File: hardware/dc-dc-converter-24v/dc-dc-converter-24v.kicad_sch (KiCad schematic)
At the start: 8 parts, among them J1 24V, J2 12V, J3 GND, J4 GND

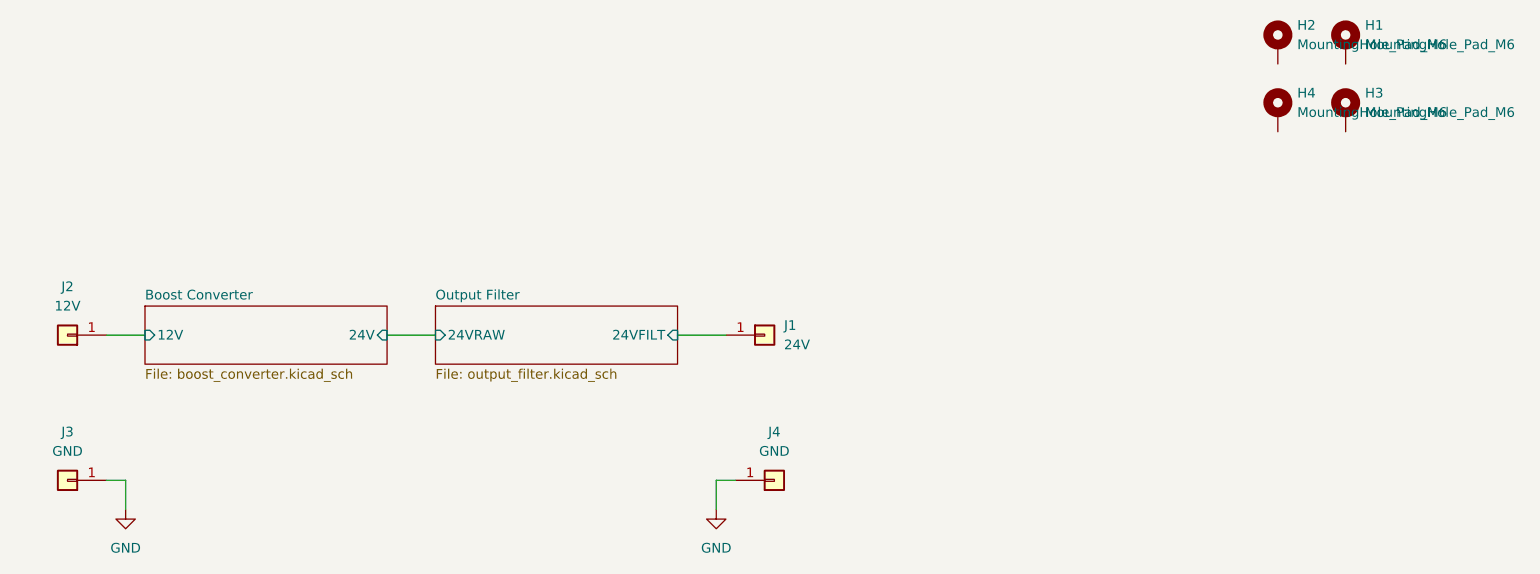
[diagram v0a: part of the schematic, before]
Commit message: create layout for DC-DC converter
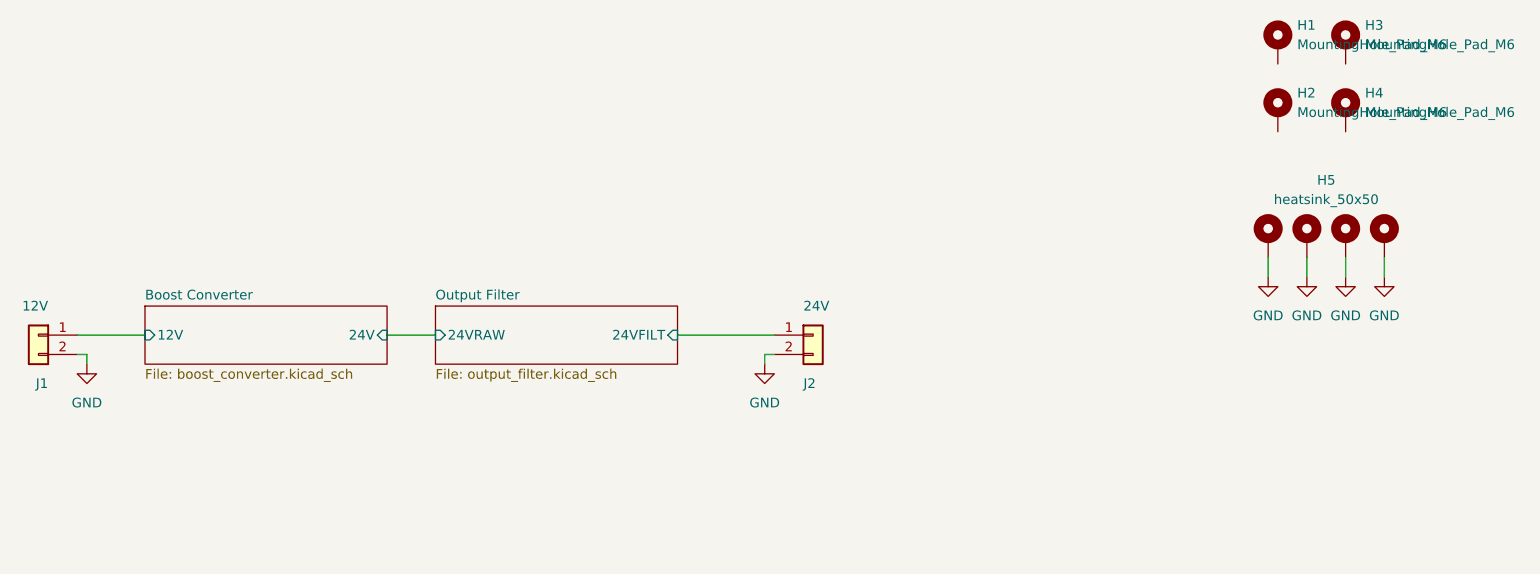
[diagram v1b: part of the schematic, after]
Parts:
- removed J1: 24V, benediktibk:Connector_M6, symbol benediktibk:Connector_M6
- removed J2: 12V, benediktibk:Connector_M6, symbol benediktibk:Connector_M6
- removed J3, J4: GND, benediktibk:Connector_M6, symbol benediktibk:Connector_M6
- added H5: heatsink_50x50, benediktibk:heatsink_50x50, symbol benediktibk:heatsink_50x50
- added J1: 12V, benediktibk:rspro_header_2pin_5_08mm, symbol benediktibk:rspro_header_2pin_5_08mm
- added J2: 24V, benediktibk:rspro_header_2pin_5_08mm, symbol benediktibk:rspro_header_2pin_5_08mm
- renumbered H2 to H1, H4 to H2, H1 to H3, H3 to H4
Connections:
- net Boost Converter/12V: now also J1.1 (Pin_1)
- net GND: now also H5.1 (GND), H5.2 (GND), H5.3 (GND), H5.4 (GND), J1.2 (Pin_2), J2.2 (Pin_2)
- net Output Filter/24VFILT: now also J2.1 (Pin_1)

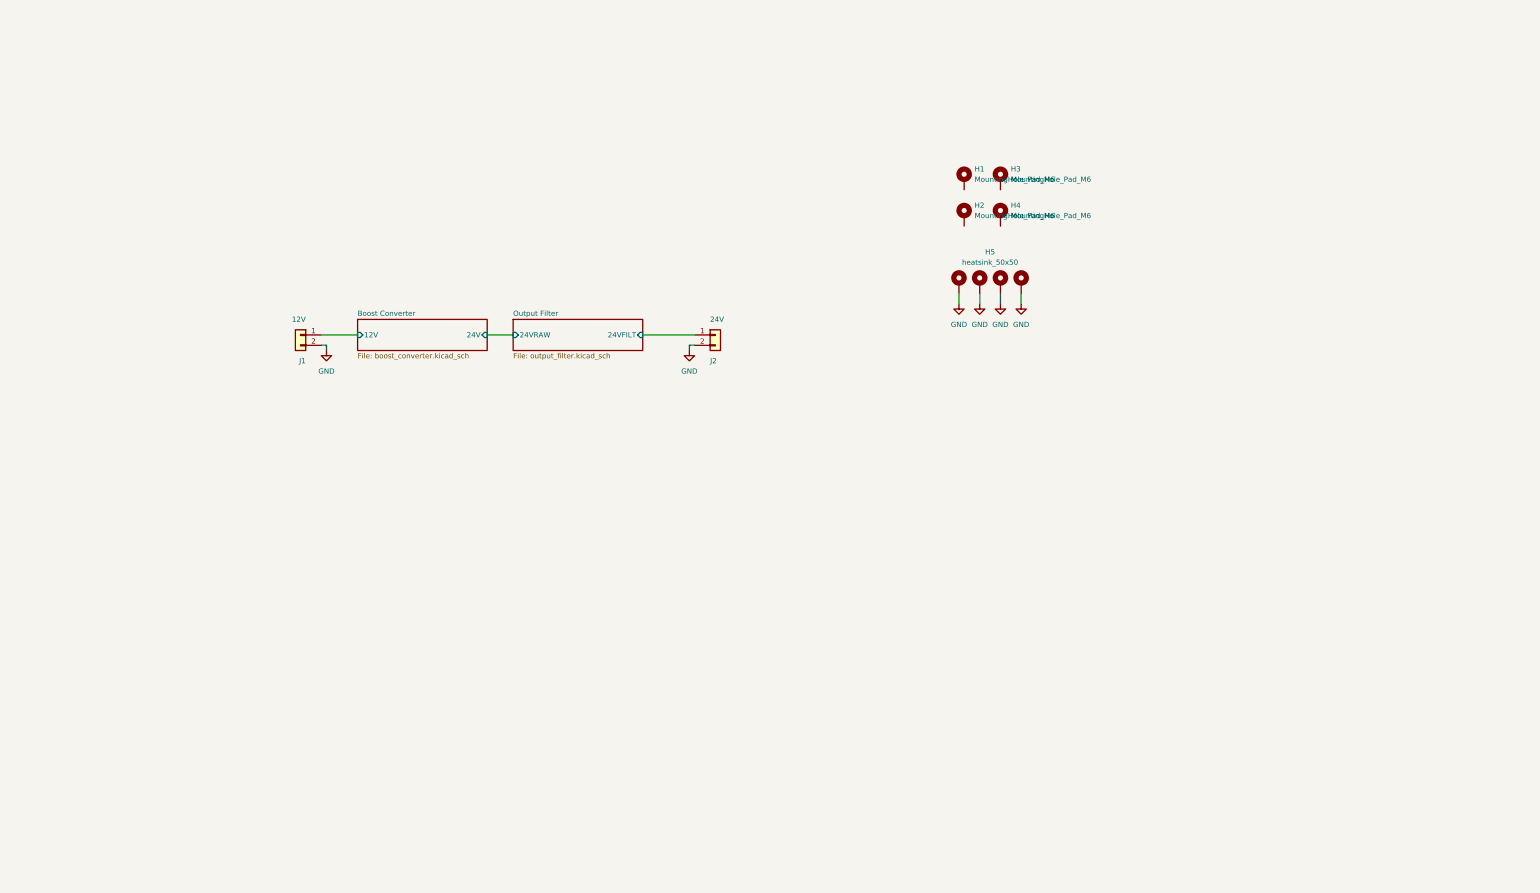
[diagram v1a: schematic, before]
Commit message: fix design errors in DC DC converter
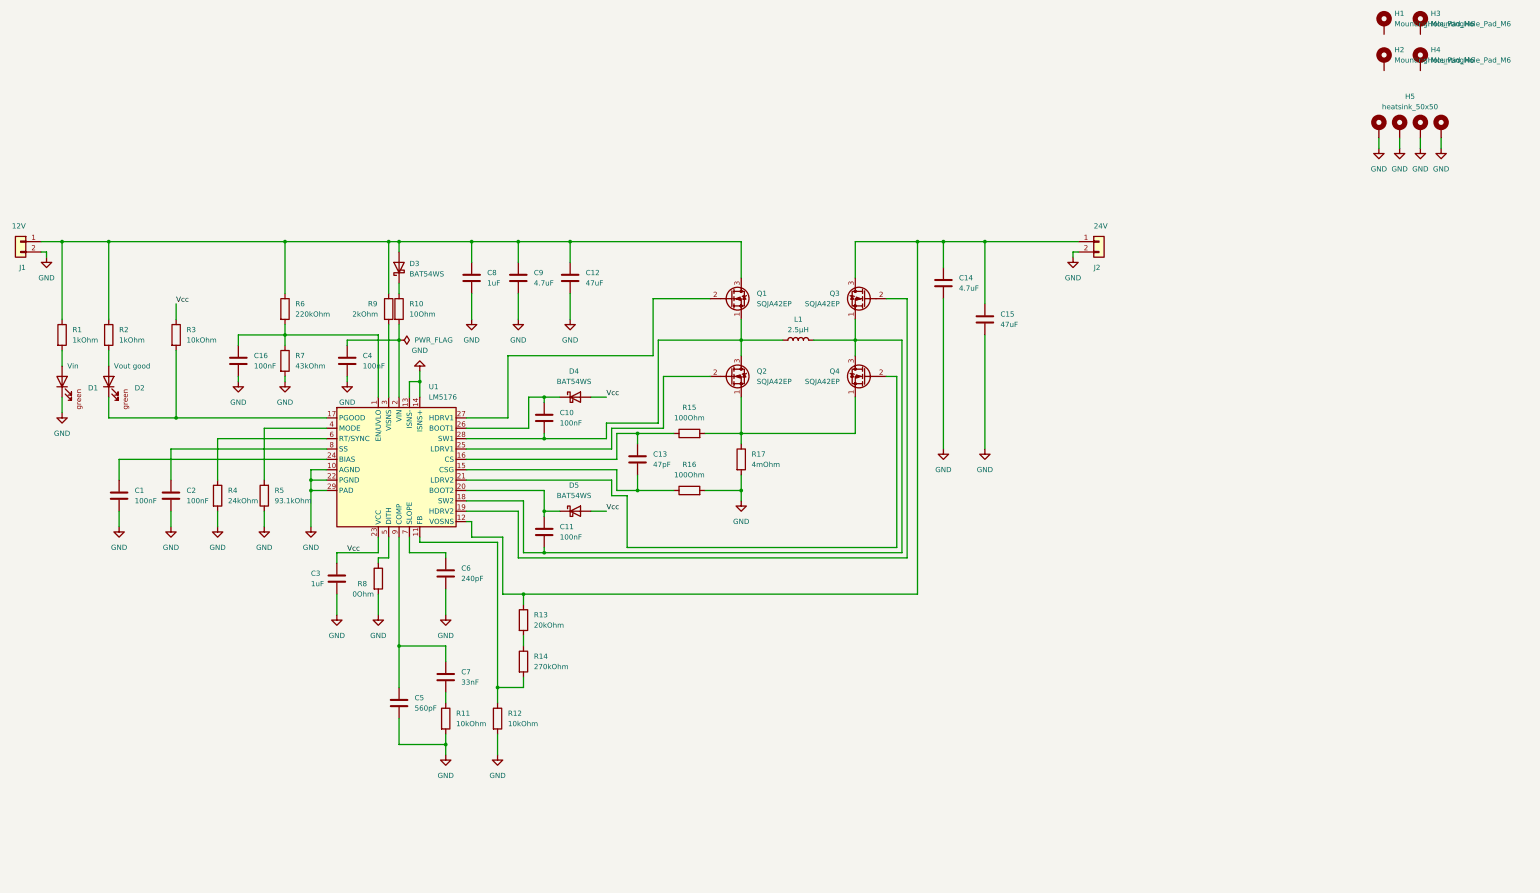
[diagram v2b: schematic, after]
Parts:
- added C1, C10, C11, C16, C2, C4: 100nF, benediktibk:C_0603_1608Metric_Pad1.08x0.95mm_HandSolder, symbol benediktibk:C_100nF_SMD_0603_50V
- added C12, C15: 47uF, benediktibk:C_1206_3216Metric_Pad1.33x1.80mm_HandSolder, symbol benediktibk:C_47uF_SMD_1206_25V_20%
- added C13: 47pF, benediktibk:C_0603_1608Metric_Pad1.08x0.95mm_HandSolder, symbol benediktibk:C_47pF_SMD_0603_100V_5%
- added C14, C9: 4.7uF, benediktibk:C_0805_2012Metric_Pad1.18x1.45mm_HandSolder, symbol benediktibk:C_4_7uF_SMD_0805_50V_10%
- added C3, C8: 1uF, benediktibk:C_0603_1608Metric_Pad1.08x0.95mm_HandSolder, symbol benediktibk:C_1uF_SMD_0603_50V_10%
- added C5: 560pF, benediktibk:C_0603_1608Metric_Pad1.08x0.95mm_HandSolder, symbol benediktibk:C_560pF_SMD_0603_50V_5%
- added C6: 240pF, benediktibk:C_0805_2012Metric_Pad1.18x1.45mm_HandSolder, symbol benediktibk:C_240pF_SMD_0805_250V_10%
- added C7: 33nF, benediktibk:C_0603_1608Metric_Pad1.08x0.95mm_HandSolder, symbol benediktibk:C_33nF_SMD_0603_50V_10%
- added D1: Vin, benediktibk:D_0603_1608Metric_Pad1.05x0.95mm_HandSolder, symbol benediktibk:LED_green_0603
- added D2: Vout good, benediktibk:D_0603_1608Metric_Pad1.05x0.95mm_HandSolder, symbol benediktibk:LED_green_0603
- added D3, D4, D5: BAT54WS, benediktibk:D_SOD-323, symbol benediktibk:BAT54WS
- added L1: 2.5µH, benediktibk:ETQP8, symbol benediktibk:L_2_5µH_30A
- added Q1, Q2, Q3, Q4: SQJA42EP, benediktibk:SQJA42EPT1_GE3, symbol benediktibk:SQJA42EP
- added R1, R2: 1kOhm, benediktibk:R_0603_1608Metric_Pad0.98x0.95mm_HandSolder, symbol benediktibk:R_1kOhm_SMD_0603_100mW_1%
- added R10: 10Ohm, benediktibk:R_0603_1608Metric_Pad0.98x0.95mm_HandSolder, symbol benediktibk:R_10Ohm_SMD_0603_100mW_1%
- added R11, R12, R3: 10kOhm, benediktibk:R_0603_1608Metric_Pad0.98x0.95mm_HandSolder, symbol benediktibk:R_10kOhm_SMD_0603_100mW_1%
- added R13: 20kOhm, benediktibk:R_0603_1608Metric_Pad0.98x0.95mm_HandSolder, symbol benediktibk:R_20kOhm_SMD_0603_100mW_1%
- added R14: 270kOhm, benediktibk:R_0603_1608Metric_Pad0.98x0.95mm_HandSolder, symbol benediktibk:R_270kOhm_SMD_0603_100mW_1%
- added R15, R16: 100Ohm, benediktibk:R_0603_1608Metric_Pad0.98x0.95mm_HandSolder, symbol benediktibk:R_100Ohm_SMD_0603_100mW_1%
- added R17: 4mOhm, benediktibk:R_2512_6332Metric_Pad1.40x3.35mm_HandSolder, symbol benediktibk:R_4mOhm_SMD_2512_2W_1%
- added R4: 24kOhm, benediktibk:R_0603_1608Metric_Pad0.98x0.95mm_HandSolder, symbol benediktibk:R_24kOhm_SMD_0603_100mW_1%
- added R5: 93.1kOhm, benediktibk:R_0603_1608Metric_Pad0.98x0.95mm_HandSolder, symbol benediktibk:R_93_1kOhm_SMD_0603_100mW_0_1%
- added R6: 220kOhm, benediktibk:R_0603_1608Metric_Pad0.98x0.95mm_HandSolder, symbol benediktibk:R_220kOhm_SMD_0603_100mW_1%
- added R7: 43kOhm, benediktibk:R_0603_1608Metric_Pad0.98x0.95mm_HandSolder, symbol benediktibk:R_43kOhm_SMD_0603_100mW_1%
- added R8: 0Ohm, benediktibk:R_0603_1608Metric_Pad0.98x0.95mm_HandSolder, symbol benediktibk:R_0Ohm_SMD_0603_100mW_0%
- added R9: 2kOhm, benediktibk:R_0603_1608Metric_Pad0.98x0.95mm_HandSolder, symbol benediktibk:R_2kOhm_SMD_0603_100mW_1%
- added U1: LM5176, benediktibk:LM5176, symbol benediktibk:LM5176
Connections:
- net GND: now also C1.2, C12.2, C14.2, C15.2, C16.2, C2.2, C3.2, C4.2, C5.2, C6.2, C8.2, C9.2, D1.1 (K), R11.2, R12.2, R16.2, R17.2, R4.2, R5.1, R7.2, R8.2, U1.10 (AGND), U1.13 (ISNS-), U1.14 (ISNS+), U1.22 (PGND), U1.29 (PAD)
- net Boost Converter/12V: no longer names the net of J1.1 (Pin_1)
- net Boost Converter/12V: now also C12.1, C8.1, C9.1, D3.2 (A), Q1.3 (D), R1.1, R2.1, R6.1, R9.1
- net Output Filter/24VFILT: no longer names the net of J2.1 (Pin_1)
- net Output Filter/24VFILT: now also C14.1, C15.1, Q3.3 (D), R13.1, U1.12 (VOSNS)
- new net: Q2.1 (S), Q4.1 (S), R15.2, R17.1
- new net: R9.2, U1.3 (VISNS)
- new net: D2.2 (A), R2.2
- new net: C11.1, D5.1 (K), U1.20 (BOOT2)
- new net: C5.1, C7.1, U1.9 (COMP)
- new net: C16.1, R6.2, R7.1, U1.1 (EN/UVLO)
- new net: C4.1, R10.2, U1.2 (VIN)
- new net: R13.2, R14.1
- new net: C7.2, R11.1
- new net: D1.2 (A), R1.2
- new net: R5.2, U1.4 (MODE)
- new net: C10.1, D4.1 (K), U1.26 (BOOT1)
- new net: R12.1, R14.2, U1.11 (FB)
- new net: C13.2, R16.1, U1.15 (CSG)
- new net: C2.1, U1.8 (SS)
- new net: D2.1 (K), R3.2, U1.17 (PGOOD)
- new net: C13.1, R15.1, U1.16 (CS)
- new net: C11.2, L1.2, Q3.1 (S), Q4.3 (D), U1.18 (SW2)
- new net: D3.1 (K), R10.1
- new net: C6.1, U1.7 (SLOPE)
- new net: C10.2, L1.1, Q1.1 (S), Q2.3 (D), U1.28 (SW1)
- new net: Q1.2 (G), U1.27 (HDRV1)
- new net: R4.1, U1.6 (RT/SYNC)
- new net: Q3.2 (G), U1.19 (HDRV2)
- new net: Q4.2 (G), U1.21 (LDRV2)
- new net: Q2.2 (G), U1.25 (LDRV1)
- new net: C1.1, U1.24 (BIAS)
- new net: R8.1, U1.5 (DITH)
- new net Vcc: C3.1, D4.2 (A), D5.2 (A), R3.1, U1.23 (VCC)
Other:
- removed sheet Boost Converter
- removed sheet Output Filter
- moved on the sheet: H1, H2, H3, H4, H5, J1, J2

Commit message: start with redesign of DC DC converter
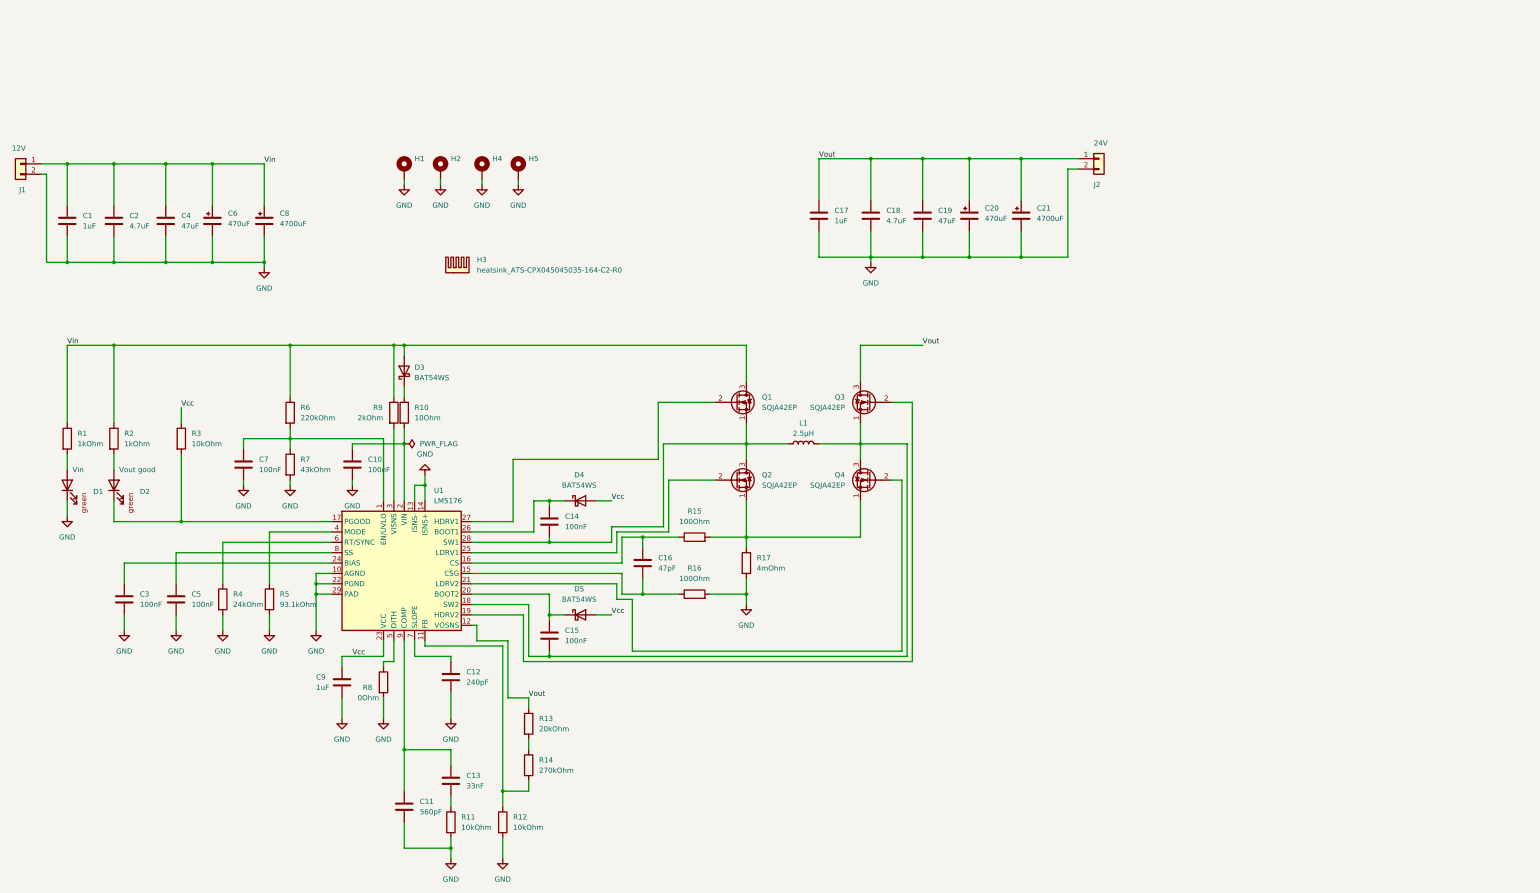
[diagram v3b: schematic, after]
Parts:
- removed C12: 47uF, benediktibk:C_1206_3216Metric_Pad1.33x1.80mm_HandSolder, symbol benediktibk:C_47uF_SMD_1206_25V_20%
- removed C8: 1uF, benediktibk:C_0603_1608Metric_Pad1.08x0.95mm_HandSolder, symbol benediktibk:C_1uF_SMD_0603_50V_10%
- removed C9: 4.7uF, benediktibk:C_0805_2012Metric_Pad1.18x1.45mm_HandSolder, symbol benediktibk:C_4_7uF_SMD_0805_50V_10%
- removed H5: heatsink_50x50, benediktibk:heatsink_50x50, symbol benediktibk:heatsink_50x50
- added C1, C17: 1uF, benediktibk:C_0603_1608Metric_Pad1.08x0.95mm_HandSolder, symbol benediktibk:C_1uF_SMD_0603_50V_10%
- added C2: 4.7uF, benediktibk:C_0805_2012Metric_Pad1.18x1.45mm_HandSolder, symbol benediktibk:C_4_7uF_SMD_0805_50V_10%
- added C20, C6: 470uF, symbol benediktibk:C_470uF_SMD_63V_20%
- added C21, C8: 4700uF, symbol benediktibk:C_4700uF_THT_50V_20%
- added C4: 47uF, benediktibk:C_1206_3216Metric_Pad1.33x1.80mm_HandSolder, symbol benediktibk:C_47uF_SMD_1206_25V_20%
- added H3: heatsink_ATS-CPX045045035-164-C2-R0, benediktibk:heatsink_984-CPX04504-164C2R0, symbol benediktibk:heatsink_ATS-CPX045045035-164-C2-R0
- renumbered C4 to C10, C5 to C11, C6 to C12, C7 to C13, C10 to C14, C11 to C15, C13 to C16, C14 to C18, C15 to C19, C1 to C3, C2 to C5, C16 to C7, C3 to C9, H3 to H4, H4 to H5
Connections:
- net GND: now also H1.1, H2.1, H4.1, H5.1, C1.2, C17.2, C2.2, C20.2, C21.2, C4.2, C6.2, C8.2
- net Vin: now reaches D3.2 (A), J1.1 (Pin_1), Q1.3 (D), R1.1, R2.1, R6.1, R9.1
- net Vin: now also C1.1, C2.1, C4.1, C6.1, C8.1
- net Vout: now reaches C18.1, C19.1, J2.1 (Pin_1), Q3.3 (D), R13.1, U1.12 (VOSNS)
- net Vout: now also C17.1, C20.1, C21.1
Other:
- moved on the sheet: C10, C11, C12, C13, C14, C15, C16, C18, C19, C3, C5, C7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

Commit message: layout DC DC converter
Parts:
- C20, C6: footprint (none) -> benediktibk:PCAP_16x16_5-ELECT_NCA-M; Mouser order number (none) -> 647-UCD1J471MNQ1MS
- C21, C8: footprint (none) -> benediktibk:CP_Radial_D22.0mm_P10.00mm_SnapIn
- renumbered H4 to H3, H5 to H4, H3 to H5
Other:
- moved on the sheet: H5
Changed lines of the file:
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@@
 			)
 		)
-		(property "Footprint" ""
+		(property "Footprint" "benediktibk:CP_Radial_D22.0mm_P10.00mm_SnapIn"
 			(at 77.1652 36.83 0)
 			(effects
@@
 	(symbol
 		(lib_id "benediktibk:heatsink_ATS-CPX045045035-164-C2-R0")
-		(at 123.19 44.45 0)
+		(at 152.4 21.59 0)
 		(unit 1)
 		(exclude_from_sim no)
@@
 		(dnp no)
 		(fields_autoplaced yes)
-		(property "Reference" "H3"
-			(at 128.27 42.5449 0)
+		(property "Reference" "H5"
+			(at 157.48 19.6849 0)
 			(effects
 				(font
@@
 		)
 		(property "Value" "heatsink_ATS-CPX045045035-164-C2-R0"
-			(at 128.27 45.0849 0)
+			(at 157.48 22.2249 0)
 			(effects
 				(font
@@
 				)
 				(justify left)
+				(hide yes)
 			)
 		)
 		(property "Footprint" "benediktibk:heatsink_984-CPX04504-164C2R0"
-			(at 123.317 34.544 0)
+			(at 152.527 11.684 0)
 			(effects
 				(font
@@
 		)
 		(property "Datasheet" "~"
-			(at 123.19 36.83 0)
+			(at 152.4 13.97 0)
 			(effects
 				(font
@@
 		)
 		(property "Description" ""
-			(at 123.19 44.45 0)
+			(at 152.4 21.59 0)
 			(effects
 				(font
@@
 		)
 		(property "Mouser order number" "984-CPX04504-164C2R0"
-			(at 123.19 44.45 0)
+			(at 152.4 21.59 0)
 			(effects
 				(font
@@
 			(project "dc-dc-converter-24v"
 				(path "/f3858519-f688-4645-91dc-9843c9d0ed53"
-					(reference "H3")
+					(reference "H5")
 					(unit 1)
 				)
@@
 		(dnp no)
 		(fields_autoplaced yes)
-		(property "Reference" "H5"
+		(property "Reference" "H4"
 			(at 140.97 17.78 0)
 			(effects
@@
 			(project "dc-dc-converter-24v"
 				(path "/f3858519-f688-4645-91dc-9843c9d0ed53"
-					(reference "H5")
+					(reference "H4")
 					(unit 1)
 				)
@@
 			)
 		)
-		(property "Footprint" ""
+		(property "Footprint" "benediktibk:PCAP_16x16_5-ELECT_NCA-M"
 			(at 249.8852 35.56 0)
 			(effects
@@
 			)
 		)
+		(property "Mouser order number" "647-UCD1J471MNQ1MS "
+			(at 248.92 31.75 0)
+			(effects
+				(font
+					(size 1.27 1.27)
+				)
+				(hide yes)
+			)
+		)
 		(pin "2"
 		)
@@
 		(dnp no)
 		(fields_autoplaced yes)
-		(property "Reference" "H4"
+		(property "Reference" "H3"
 			(at 132.08 17.78 0)
 			(effects
@@
 			(project "dc-dc-converter-24v"
 				(path "/f3858519-f688-4645-91dc-9843c9d0ed53"
-					(reference "H4")
+					(reference "H3")
 					(unit 1)
 				)
@@
 			)
 		)
-		(property "Footprint" ""
+		(property "Footprint" "benediktibk:PCAP_16x16_5-ELECT_NCA-M"
 			(at 64.4652 36.83 0)
 			(effects
@@
 			)
 		)
+		(property "Mouser order number" "647-UCD1J471MNQ1MS "
+			(at 63.5 33.02 0)
+			(effects
+				(font
+					(size 1.27 1.27)
+				)
+				(hide yes)
+			)
+		)
 		(pin "2"
 		)
@@
 			)
 		)
-		(property "Footprint" ""
+		(property "Footprint" "benediktibk:CP_Radial_D22.0mm_P10.00mm_SnapIn"
 			(at 262.5852 35.56 0)
 			(effects
